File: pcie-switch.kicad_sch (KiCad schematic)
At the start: 44 parts, among them J1 Tag-Connect_TC2050-IDC-NL_2x5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, U1 PI7C9X3G606GP

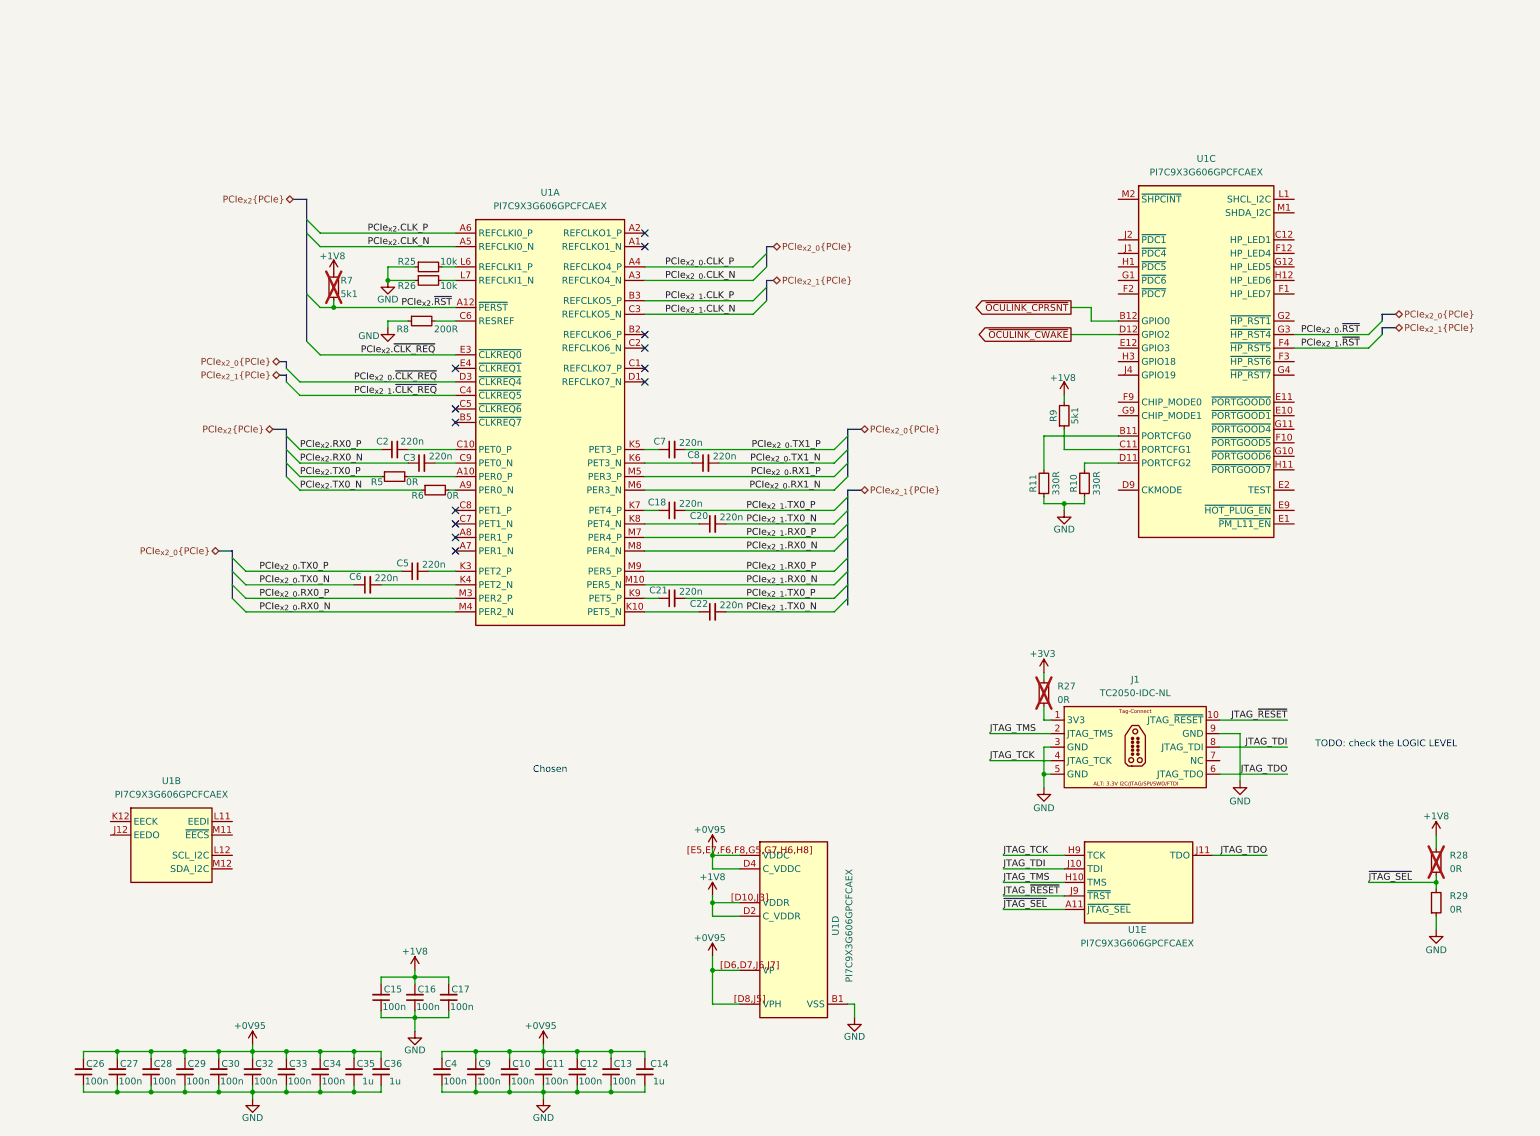
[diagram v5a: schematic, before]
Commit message: [#100765] Add LLC to I2C of the PCIe switch
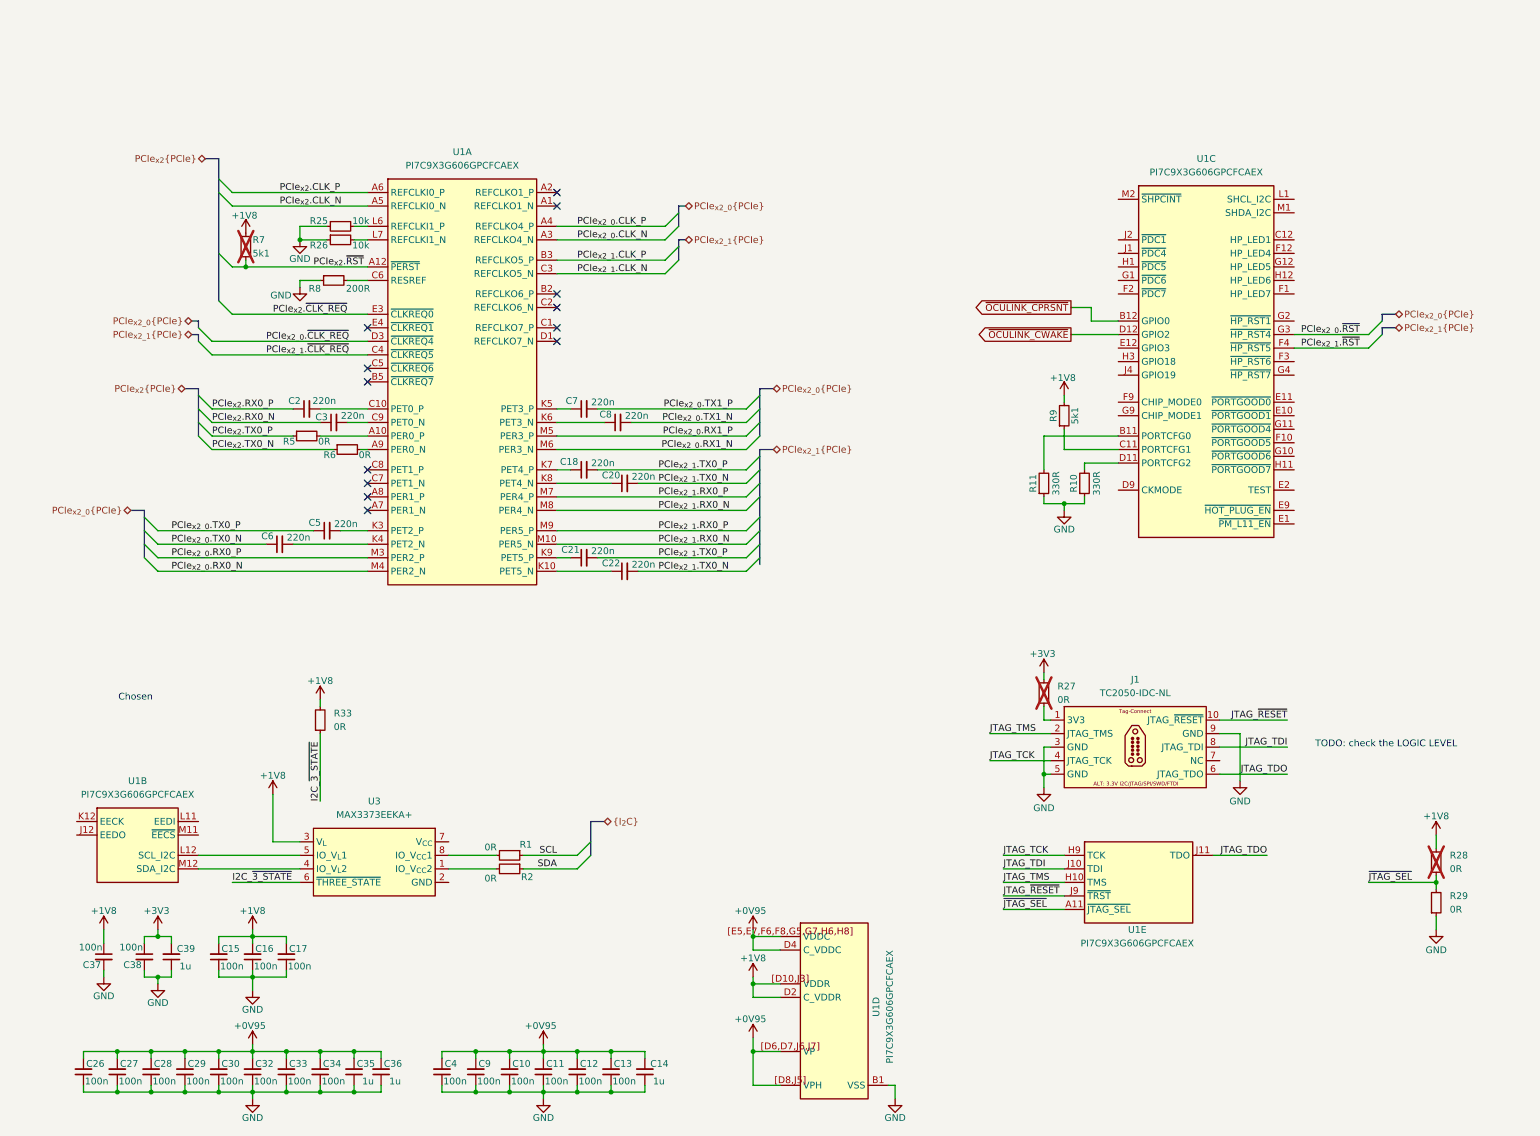
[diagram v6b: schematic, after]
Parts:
- added C37, C38: C_100n_0402, antmicro-footprints:C_0402_1005Metric, symbol antmicroCapacitors0402:C_100n_0402
- added C39: C_1u_0402, antmicro-footprints:C_0402_1005Metric, symbol antmicroCapacitors0402:C_1u_0402
- added R1, R2, R33: R_0R_0402, antmicro-footprints:R_0402_1005Metric, symbol antmicroResistors0402:R_0R_0402
- added U3: MAX3373EEKA+, antmicro-footprints:SOT-23-8, symbol antmicroLogicTranslatorsLevelShifters:MAX3373EEKA+
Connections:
- net +1V8: now also C37.1, R33.2, U3.3 (V_{L})
- net +3V3: now also C38.1, C39.2
- net GND: now also C37.2, C38.2, C39.1
- net at U1.L12 (SCL_I2C): now also U3.5 (IO_V_{L}1)
- net at U1.M12 (SDA_I2C): now also U3.4 (IO_V_{L}2)
- new net: R2.2, U3.1 (IO_V_{CC}2)
- new net: R1.2, U3.8 (IO_V_{CC}1)
- new net I2C_~{3_STATE}: R33.1, U3.6 (~{THREE_STATE})
- new net SCL: R1.1
- new net SDA: R2.1
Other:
- moved on the sheet: C15, C16, C17, C18, C2, C20, C21, C22, C3, C5, C6, C7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

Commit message: [#100765] Add Control LEDs, update Power section
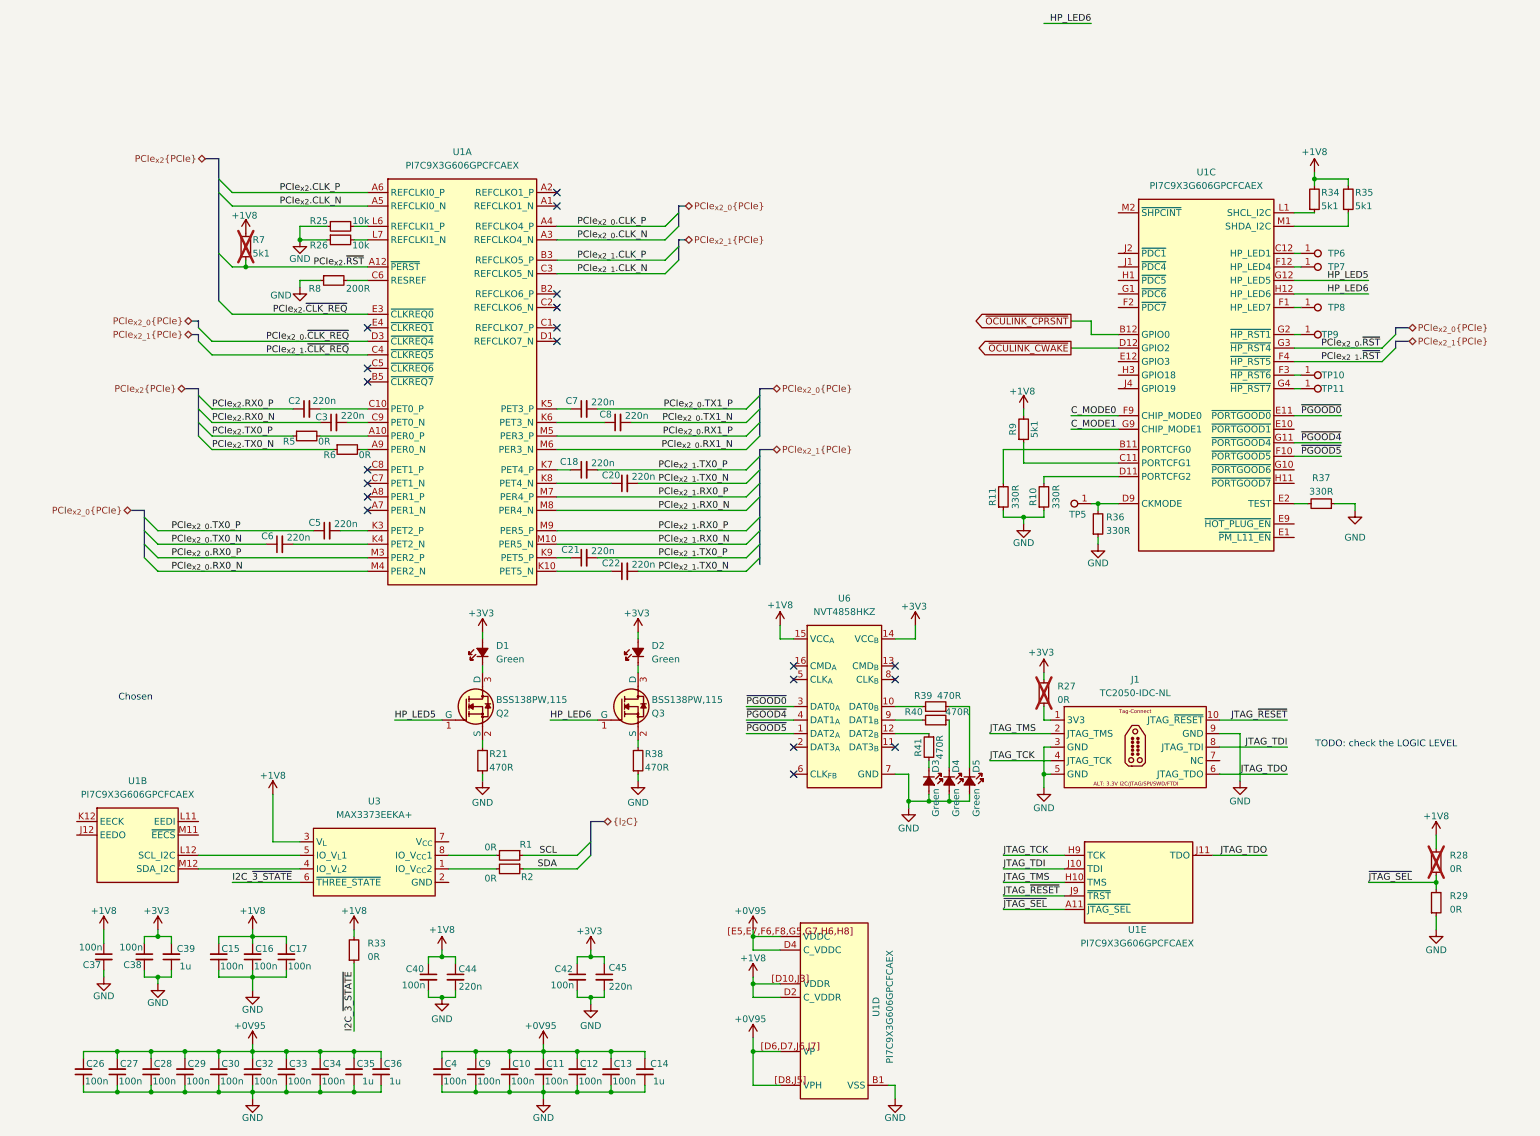
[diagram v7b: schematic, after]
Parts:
- added C40, C42: C_100n_16V_X7R_0402, antmicro-footprints:C_0402_1005Metric, symbol antmicroCapacitors0402:C_100n_16V_X7R_0402
- added C44, C45: C_220n_0402, antmicro-footprints:C_0402_1005Metric, symbol antmicroCapacitors0402:C_220n_0402
- added D1, D2, D3, D4, D5: LED_G_0603_LG_L29K-G2J1-24-Z, antmicro-footprints:LED_0603_1608Metric_G, symbol antmicroLEDIndicationDiscrete:LED_G_0603_LG_L29K-G2J1-24-Z
- added Q2, Q3: BSS138PW,115, antmicro-footprints:SC70-3, symbol antmicroTransistorsFETsMOSFETsSingle:BSS138PW,115
- added R21, R38, R39, R40, R41: R_470R_0402, antmicro-footprints:R_0402_1005Metric, symbol antmicroResistors0402:R_470R_0402
- added R34, R35: R_5k1_0402, antmicro-footprints:R_0402_1005Metric, symbol antmicroResistors0402:R_5k1_0402
- added R36, R37: R_330R_0402, antmicro-footprints:R_0402_1005Metric, symbol antmicroResistors0402:R_330R_0402
- added TP10, TP11, TP5, TP6, TP7, TP8, TP9: TP_1mm_SMD, antmicro-footprints:TP_SMD_1mm, symbol antmicroTestPoints:TP_1mm_SMD
- added U6: NVT4858_XQFN, antmicro-footprints:SOT1161-2, symbol antmicroLogicTranslatorsLevelShifters:NVT4858_XQFN
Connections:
- net +1V8: now also C40.1, C44.1, R34.2, R35.2, U6.15 (VCC_{A})
- net +3V3: now also C42.1, C45.1, D1.2 (A), D2.2 (A), U6.14 (VCC_{B})
- net GND: now also C40.2, C42.2, C44.2, C45.2, D3.2 (A), D4.2 (A), D5.2 (A), R21.1, R36.1, R37.1, R38.1, U6.7 (GND)
- net at U1.C12 (HP_LED1): now also TP6.1
- net at U1.D9 (CKMODE): now also R36.2, TP5.1
- net ~{PGOOD0}: now reaches U1.E11 (~{PORTGOOD0})
- net ~{PGOOD0}: now also U6.3 (DAT0_{A})
- net at U1.E2 (TEST): now also R37.2
- net at U1.F1 (HP_LED7): now also TP8.1
- net ~{PGOOD5}: now reaches U1.F10 (~{PORTGOOD5})
- net ~{PGOOD5}: now also U6.1 (DAT2_{A})
- net at U1.F12 (HP_LED4): now also TP7.1
- net at U1.F3 (~{HP_RST6}): now also TP10.1
- net C_MODE0: now reaches U1.F9 (CHIP_MODE0)
- net ~{PGOOD4}: now reaches U1.G11 (~{PORTGOOD4})
- net ~{PGOOD4}: now also U6.4 (DAT1_{A})
- net HP_LED5: now reaches U1.G12 (HP_LED5)
- net HP_LED5: now also Q2.1 (G)
- net at U1.G2 (~{HP_RST1}): now also TP9.1
- net at U1.G4 (~{HP_RST7}): now also TP11.1
- net C_MODE1: now reaches U1.G9 (CHIP_MODE1)
- net HP_LED6: now reaches U1.H12 (HP_LED6)
- net HP_LED6: now also Q3.1 (G)
- net at U1.L1 (SHCL_I2C): now also R34.1
- net at U1.M1 (SHDA_I2C): now also R35.1
- new net: D1.1 (C), Q2.3 (D)
- new net: D5.1 (C), R39.1
- new net: R39.2, U6.10 (DAT0_{B})
- new net: R41.1, U6.12 (DAT2_{B})
- new net: R40.2, U6.9 (DAT1_{B})
- new net: Q2.2 (S), R21.2
- new net: D3.1 (C), R41.2
- new net: D2.1 (C), Q3.3 (D)
- new net: Q3.2 (S), R38.2
- new net: D4.1 (C), R40.1
- no-connect marks 13 -> 20
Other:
- moved on the sheet: R10, R11, R33, R9, U1C

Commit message: [#100765] Work on schematic
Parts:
- removed J1: Tag-Connect_TC2050-IDC-NL_2x5_P1.27mm, antmicro-footprints:Tag-Connect_TC2050-IDC-NL_2x5_P1.27mm, symbol antmicroTestPoints:Tag-Connect_TC2050-IDC-NL_2x5_P1.27mm
- removed R27: R_0R_0402, antmicro-footprints:R_0402_1005Metric, symbol antmicroResistors0402:R_0R_0402
- added R42, R43: R_330R_0402, antmicro-footprints:R_0402_1005Metric, symbol antmicroResistors0402:R_330R_0402
- added TP12, TP13, TP14: TP_1mm_SMD, antmicro-footprints:TP_SMD_1mm, symbol antmicroTestPoints:TP_1mm_SMD
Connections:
- net +3V3: now also U3.7 (V_{CC})
- net GND: now also U3.2 (GND), R42.1, R43.1
- net at U1.E12 (GPIO3): now also TP12.1
- net at U1.H1 (~{PDC5}): now also R43.2
- net at U1.H3 (GPIO18): now also TP13.1
- net at U1.J1 (~{PDC4}): now also R42.2
- net at U1.J4 (GPIO19): now also TP14.1
- net MISO: now reaches U1.J12 (EEDO)
- net MISO: now also U1.M11 (~{EECS})
- net SCK: now reaches U1.K12 (EECK)
- net MOSI: now reaches U1.L11 (EEDI)
- no-connect marks 20 -> 27
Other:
- note added: "~{JTAG_SEL}"
- note removed: "TODO: check the LOGIC LEVEL"
- moved on the sheet: D1, D2, D3, D4, D5, Q2, Q3, R1, R2, R21, R38, R39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
